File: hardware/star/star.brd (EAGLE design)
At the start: 139.4 x 187.9 mm, 172 parts, among them IC1 MAX481CSA, IC2 LD117AS12TR, IC22 LD117AS12TR, IC3 74HCT08D, IC4 7404D, IC8 MAX481CSA, K1 T90-12VDC-TL-A, K2 T90-12VDC-TL-A, K3 T90-12VDC-TL-A, K5 AQG22110, K6 AQG22110, Q1 35A/25V/8.5mΩ, Q2 35A/25V/8.5mΩ, Q3 35A/25V/8.5mΩ, Q4 35A/25V/8.5mΩ, T1 T_PNP_MMBT5401_CHANGJ_SOT23-B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, T2 T_PNP_MMBT5401_CHANGJ_SOT23-B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, T3 T_PNP_MMBT5401_CHANGJ_SOT23-B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, T4 T_PNP_MMBT5401_CHANGJ_SOT23-B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, U1 TCLT1600

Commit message: Lots of updates
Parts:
- removed C10, C9: C_100UF/6.3V_1206, JLC PCB Basic Parts_loc:C1206
- removed C2, C5: 10uf, rcl:C0603
- removed C24, C26, C4: 1uf, rcl:C0805
- removed F2: 2920L200, 2920L200:SMD050F
- removed JP2: (no value), pinhead:2X02
- removed U$2: ZK-SJVA-4X, Nova:ZK-SJVA-4X
- removed U$3: EPS-25, Nova:EPS-25
- added EPP-120S-24: EPP-120S, Nova:EPS-25
- added NID35-12, NID35-5: NID35, Nova:NID35
- added SKA15B-05: SKA15B, Nova:SKA15B
- IC2: value LD117AS12TR -> 74HCT08D; device v-reg:SOT223 -> 74xx-eu:SO14
- R62: value R_7.5K_0603 -> R_15K_0603
- moved C25 111.1 mm to (134.6, 148.0)
- moved IC2 55.0 mm to (83.2, 65.4)
- moved JP1 51.6 mm to (7.62, 67.3)
- moved C33 35.4 mm to (137.2, 27.9), turned to 90 degrees
- moved I2C 32.4 mm to (132.1, 13.3), turned to 180 degrees
- moved OVERRIDE_EN2 32.1 mm to (126.4, 111.1)
- moved R50 32.0 mm to (121.9, 109.9), turned to 270 degrees
- moved OVERRIDE_EN 31.9 mm to (132.7, 110.5)
- moved IC8 30.5 mm to (133.3, 27.9), turned to 180 degrees
- moved JTAG 28.4 mm to (120.0, 2.54), turned to 180 degrees
- moved 5V_CTRL_LAZERS 20.3 mm to (132.7, 52.7)
- moved C14 20.3 mm to (137.2, 86.4)
- moved D4 20.3 mm to (123.8, 100.3)
- moved IC1 20.3 mm to (133.3, 86.4)
- moved R1 20.3 mm to (137.2, 78.7)
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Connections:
- removed net +14V: C25.1, D14.C, D17.A, FIRE_OUT.3, U$2.OUT+
- removed net N$59: F2.1, POWER_IN.4
- new net +24V: C25.1, D14.C, D17.A, EPP-120S-24.OUT+, FIRE_OUT.3, NID35-12.VIN1, NID35-12.VIN2, NID35-5.VIN1, NID35-5.VIN2, SKA15B-05.+VIN
- new net N$60: IC2.3, Q4.1
- net +12V: now also NID35-12.VOUT1, NID35-12.VOUT2, NID35-12.VOUT3, NID35-12.VOUT4, POWER_IN.4; no longer C2.1, C24.1, C28.+, C35.1, C4.1, C6.1, C89.+, F2.2, IC2.3, IC22.3, U$2.IN+
- net +3V3: now also C28.+, IC2.14
- net +5V: now also C35.1, C6.1, C89.+, IC22.3, NID35-5.VOUT1, NID35-5.VOUT2, NID35-5.VOUT3, NID35-5.VOUT4; no longer C10.1, C5.1, C9.1, IC2.4
- net +5V/2: now also SKA15B-05.+VOUT; no longer C26.1, U$3.OUT+
- net 120_LINE: now also EPP-120S-24.IN-; no longer U$3.IN-
- net 120_NEUTRAL: now also EPP-120S-24.IN+; no longer U$3.IN+
- net 15: now also IC2.2
- net 26_BOOM_IGNITER: now also IC2.1; no longer Q4.1
- net GND: now also EPP-120S-24.OUT-, IC2.7, NID35-12.COM1, NID35-12.COM2, NID35-5.COM1, NID35-5.COM2, SKA15B-05.-VIN; no longer C10.2, C2.2, C24.2, C4.2, C5.2, C9.2, IC2.1, JP2.1, JP2.2, JP2.3, JP2.4, U$2.IN-, U$2.OUT-
- net GND3: now also SKA15B-05.-VOUT; no longer C26.2, U$3.OUT-
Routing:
- net +24V: track 0.00 -> 265.2 mm
- net +12V: track 329.4 -> 149.8 mm
- net +14V: track 106.5 -> 0.00 mm
- net +5V/2: track 128.6 -> 42.2 mm
- net +5V: track 104.2 -> 36.8 mm
- net GND3: track 148.6 -> 86.4 mm
- net +3V3: track 53.8 -> 0.00 mm
- net 120_NEUTRAL: track 180.5 -> 164.3 mm
- net N$59: track 10.2 -> 0.00 mm
- net 120_LINE: track 153.1 -> 146.7 mm
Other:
- board text added: "3v3"
- board text added: "3v3 5v 12v Enable"
- board text added: "ISOLATED 5V"
- board text removed: "12v"
- board text removed: "3v 5v 12v Enable"

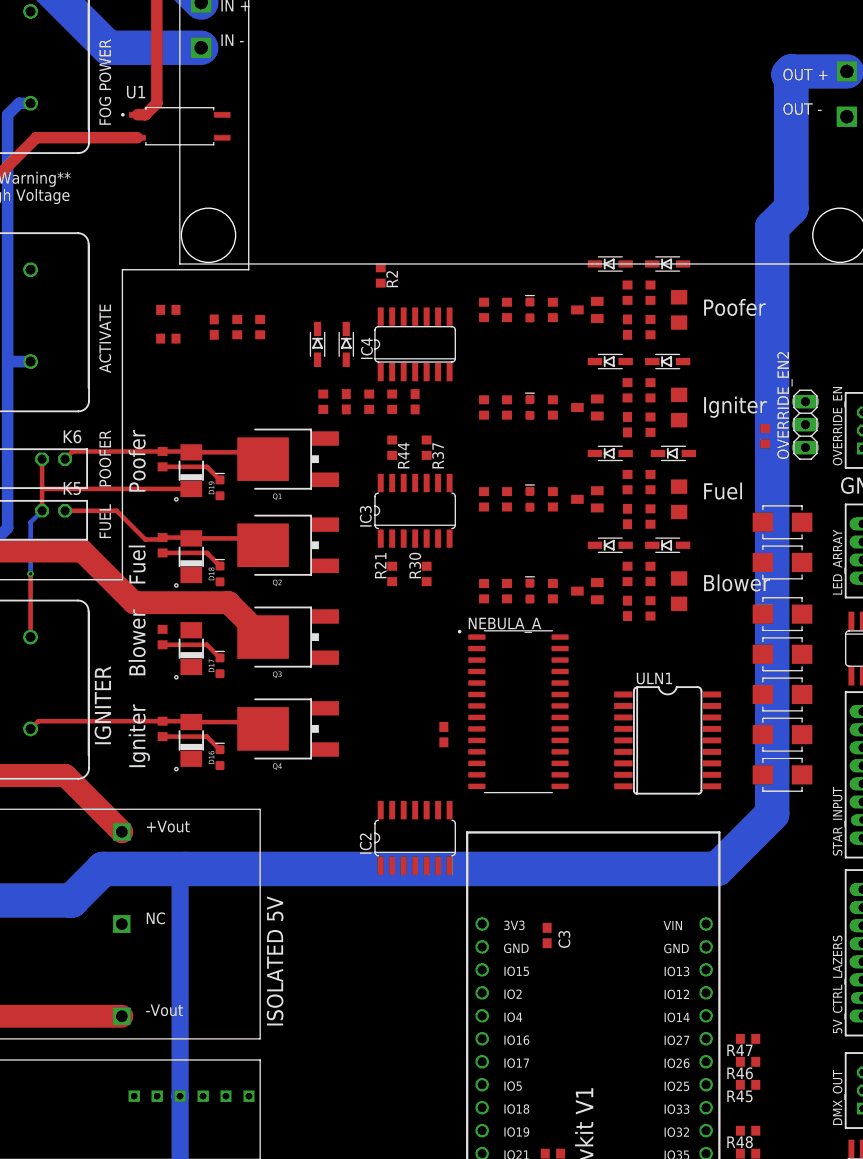
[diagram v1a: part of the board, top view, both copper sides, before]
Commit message: update few traces
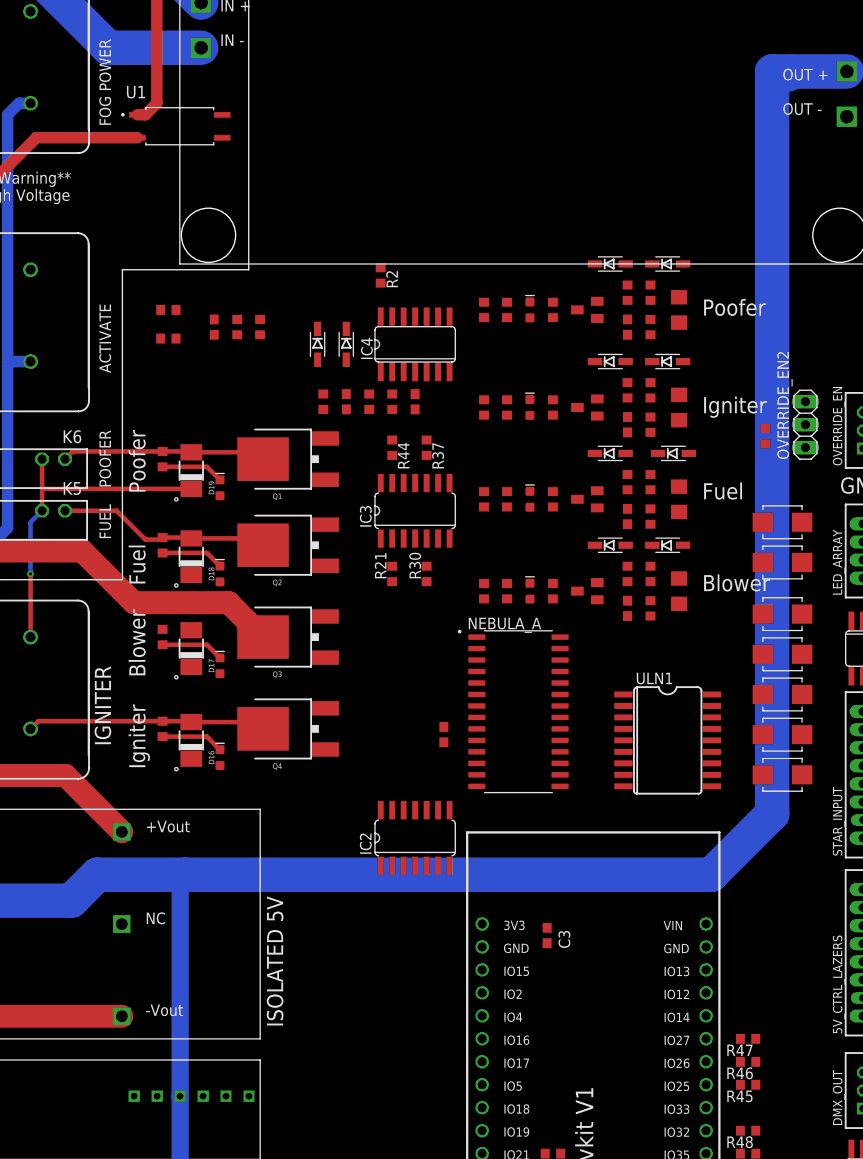
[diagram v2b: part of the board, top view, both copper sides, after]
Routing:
- net +24V: track 265.2 -> 265.8 mm
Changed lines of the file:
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@@
 <contactref element="NID35-12" pad="VIN1"/>
 <wire x1="130.945" y1="150.205" x2="124.805" y2="150.205" width="3.81" layer="16"/>
+<wire x1="124.805" y1="150.205" x2="122.682" y2="150.205" width="3.81" layer="16"/>
 <wire x1="124.46" y1="149.86" x2="124.805" y2="150.205" width="3.81" layer="16"/>
-<wire x1="124.805" y1="150.205" x2="124.805" y2="135.0835625" width="3.81" layer="16"/>
-<wire x1="124.805" y1="135.0835625" x2="122.682" y2="132.9605625" width="3.81" layer="16"/>
-<wire x1="122.682" y1="132.9605625" x2="122.682" y2="68.072" width="3.81" layer="16"/>
+<wire x1="122.682" y1="150.205" x2="122.682" y2="68.072" width="3.81" layer="16"/>
 <wire x1="45.1617125" y1="58.48" x2="30.54" y2="58.48" width="3.81" layer="16"/>
-<wire x1="116.588" y1="61.978" x2="57.785" y2="61.978" width="3.81" layer="16"/>
-<wire x1="57.785" y1="61.978" x2="48.6597125" y2="61.978" width="3.81" layer="16"/>
-<wire x1="48.6597125" y1="61.978" x2="45.1617125" y2="58.48" width="3.81" layer="16"/>
-<wire x1="122.682" y1="68.072" x2="116.588" y2="61.978" width="3.81" layer="16"/>
-<wire x1="57.18" y1="36.845" x2="57.18" y2="61.373" width="1.905" layer="16"/>
-<wire x1="57.18" y1="61.373" x2="57.785" y2="61.978" width="1.905" layer="16"/>
+<wire x1="115.953" y1="61.343" x2="57.785" y2="61.343" width="3.81" layer="16"/>
+<wire x1="57.785" y1="61.343" x2="48.0247125" y2="61.343" width="3.81" layer="16"/>
+<wire x1="48.0247125" y1="61.343" x2="45.1617125" y2="58.48" width="3.81" layer="16"/>
+<wire x1="122.682" y1="68.072" x2="115.953" y2="61.343" width="3.81" layer="16"/>
+<wire x1="57.18" y1="36.845" x2="57.18" y2="60.738" width="1.905" layer="16"/>
+<wire x1="57.18" y1="60.738" x2="57.785" y2="61.343" width="1.905" layer="16"/>
 <wire x1="57.18" y1="36.845" x2="57.18" y2="23.51" width="1.905" layer="16"/>
 <contactref element="D14" pad="C"/>
@@
 <wire x1="54.64" y1="36.845" x2="57.18" y2="36.845" width="0" layer="19" extent="1-1"/>
 <wire x1="54.64" y1="23.51" x2="57.18" y2="23.51" width="0" layer="19" extent="1-1"/>
-<wire x1="134.62" y1="148.905" x2="130.945" y2="150.205" width="0" layer="19" extent="1-1"/>
+<wire x1="134.62" y1="148.905" x2="124.805" y2="150.205" width="0" layer="19" extent="1-1"/>
 </signal>
 <signal name="N$60">

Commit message: Manual routing complete
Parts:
- added X1: MKDSN1,5/2-5,08, con-phoenix-508-jm:MKDSN1,5/2-5,08
- moved POWER_IN 20.3 mm to (7.62, 45.1)
- moved C1 5.08 mm to (125.1, 20.3)
- moved C3 5.08 mm to (102.9, 54.6)
- moved R26 5.08 mm to (103.5, 22.9)
- moved R27 5.08 mm to (103.5, 30.5)
- moved R45 5.08 mm to (125.1, 38.1)
- moved R46 5.08 mm to (125.1, 40.6)
- moved R47 5.08 mm to (125.1, 43.2)
- moved R48 5.08 mm to (125.1, 33.0)
- moved R49 5.08 mm to (125.1, 30.5)
- moved U$1 5.08 mm to (109.2, 33.0)
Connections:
- net +24V: now also X1.2
- net 26_BOOM_IGNITER: now also Q4.1; no longer IC2.1
- net 32_BOOM_BLOWER: now also IC2.1; no longer Q3.1
- net GND: now also X1.1
- net N$60: now also Q3.1; no longer Q4.1
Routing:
- net +5V: track 36.8 -> 218.3 mm
- net GND3: track 86.4 -> 0.00 mm
- net +24V: track 265.8 -> 320.1 mm
- net +3V3: track 0.00 -> 50.2 mm
- net +12V: track 149.8 -> 171.9 mm
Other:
- board text added: "GND 24v"
- board text removed: "120vac IN"
- board text removed: "GND 5v/2"

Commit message: starbase v02
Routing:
- net +3V3: track 50.2 -> 504.9 mm, vias 0 -> 11
- net GND: track 0.30 -> 426.1 mm, vias 0 -> 12
- net +5V: track 218.3 -> 501.0 mm, vias 1 -> 3
- net EXP_ULN1: track 0.00 -> 198.2 mm, vias 0 -> 3
- net LOCAL_EN: track 0.00 -> 175.9 mm, vias 0 -> 4
- net EXP_ULN0: track 0.00 -> 164.1 mm, vias 0 -> 2
- net +12V: track 171.9 -> 327.7 mm, vias 0 -> 5
- net EN_STATUS: track 0.00 -> 155.8 mm, vias 0 -> 2
- net A0: track 0.00 -> 148.4 mm, vias 0 -> 2
- net 19: track 0.00 -> 128.0 mm
- net 18: track 0.00 -> 117.9 mm
- net 21/SDA: track 0.00 -> 103.2 mm
- net 22/SCL: track 0.00 -> 93.9 mm, vias 0 -> 1
- net 25_POOFER: track 0.00 -> 91.4 mm, vias 0 -> 2
- net N$4: track 0.00 -> 89.9 mm, vias 0 -> 2
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
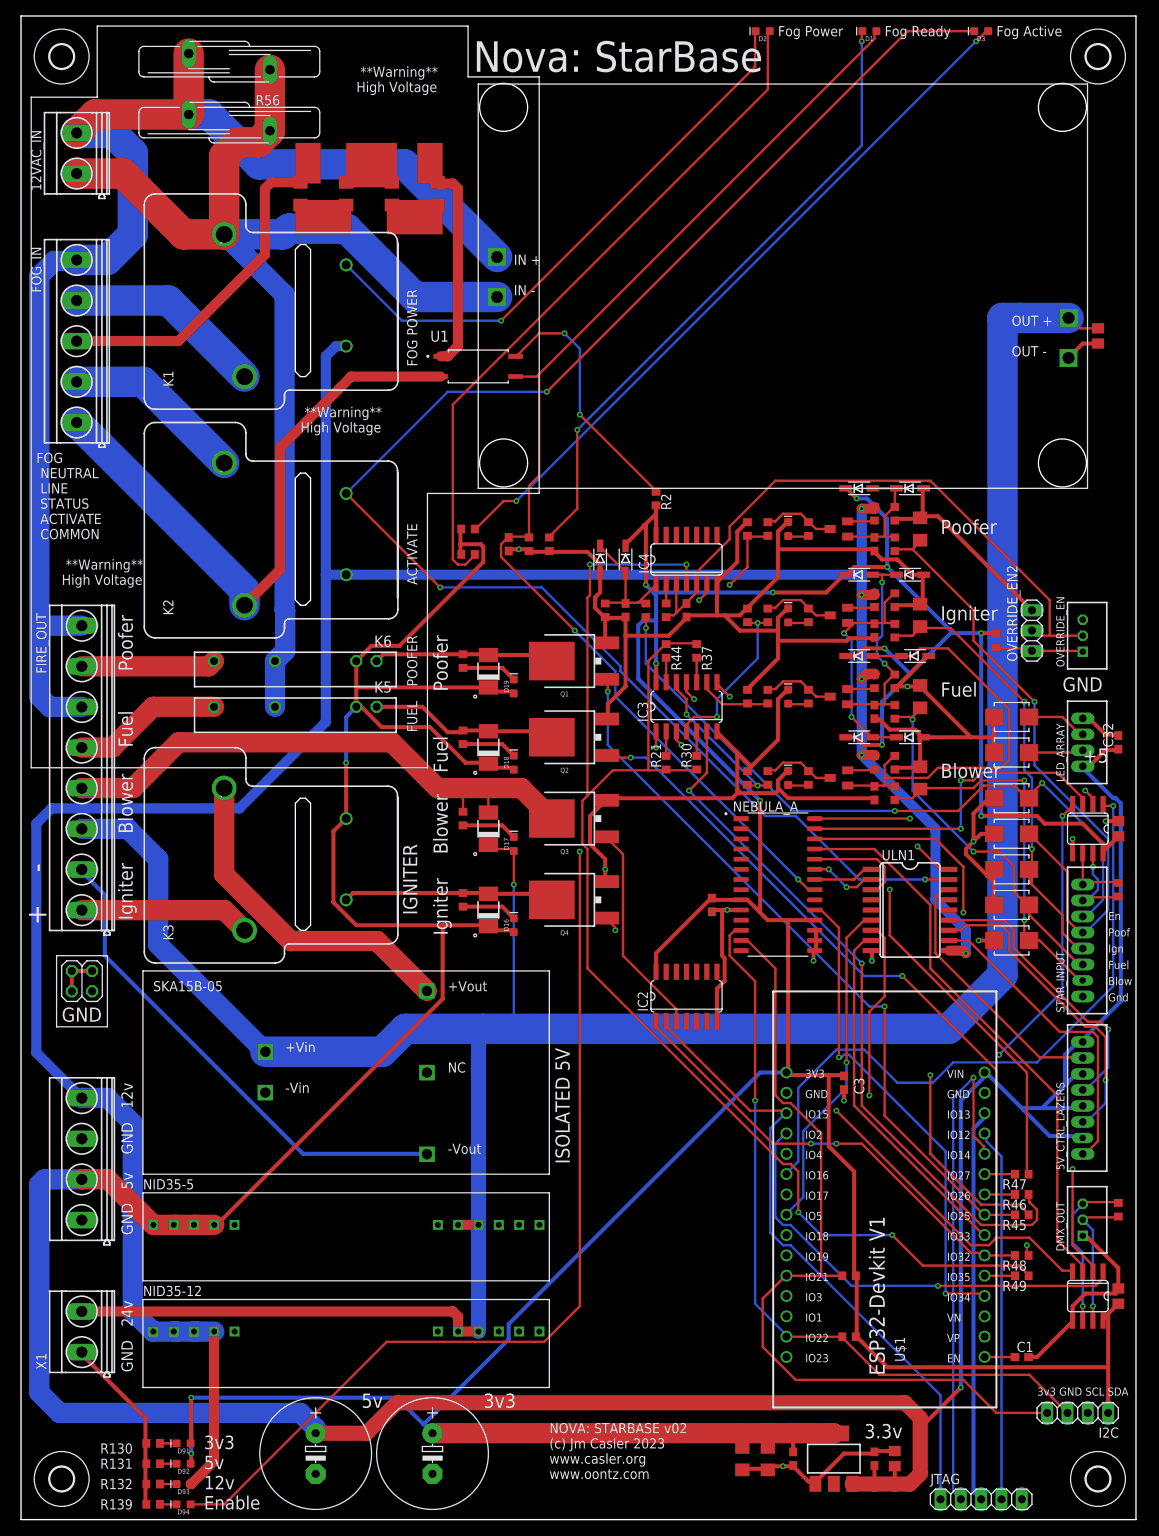
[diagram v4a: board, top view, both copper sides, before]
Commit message: swap to schmitt trigger
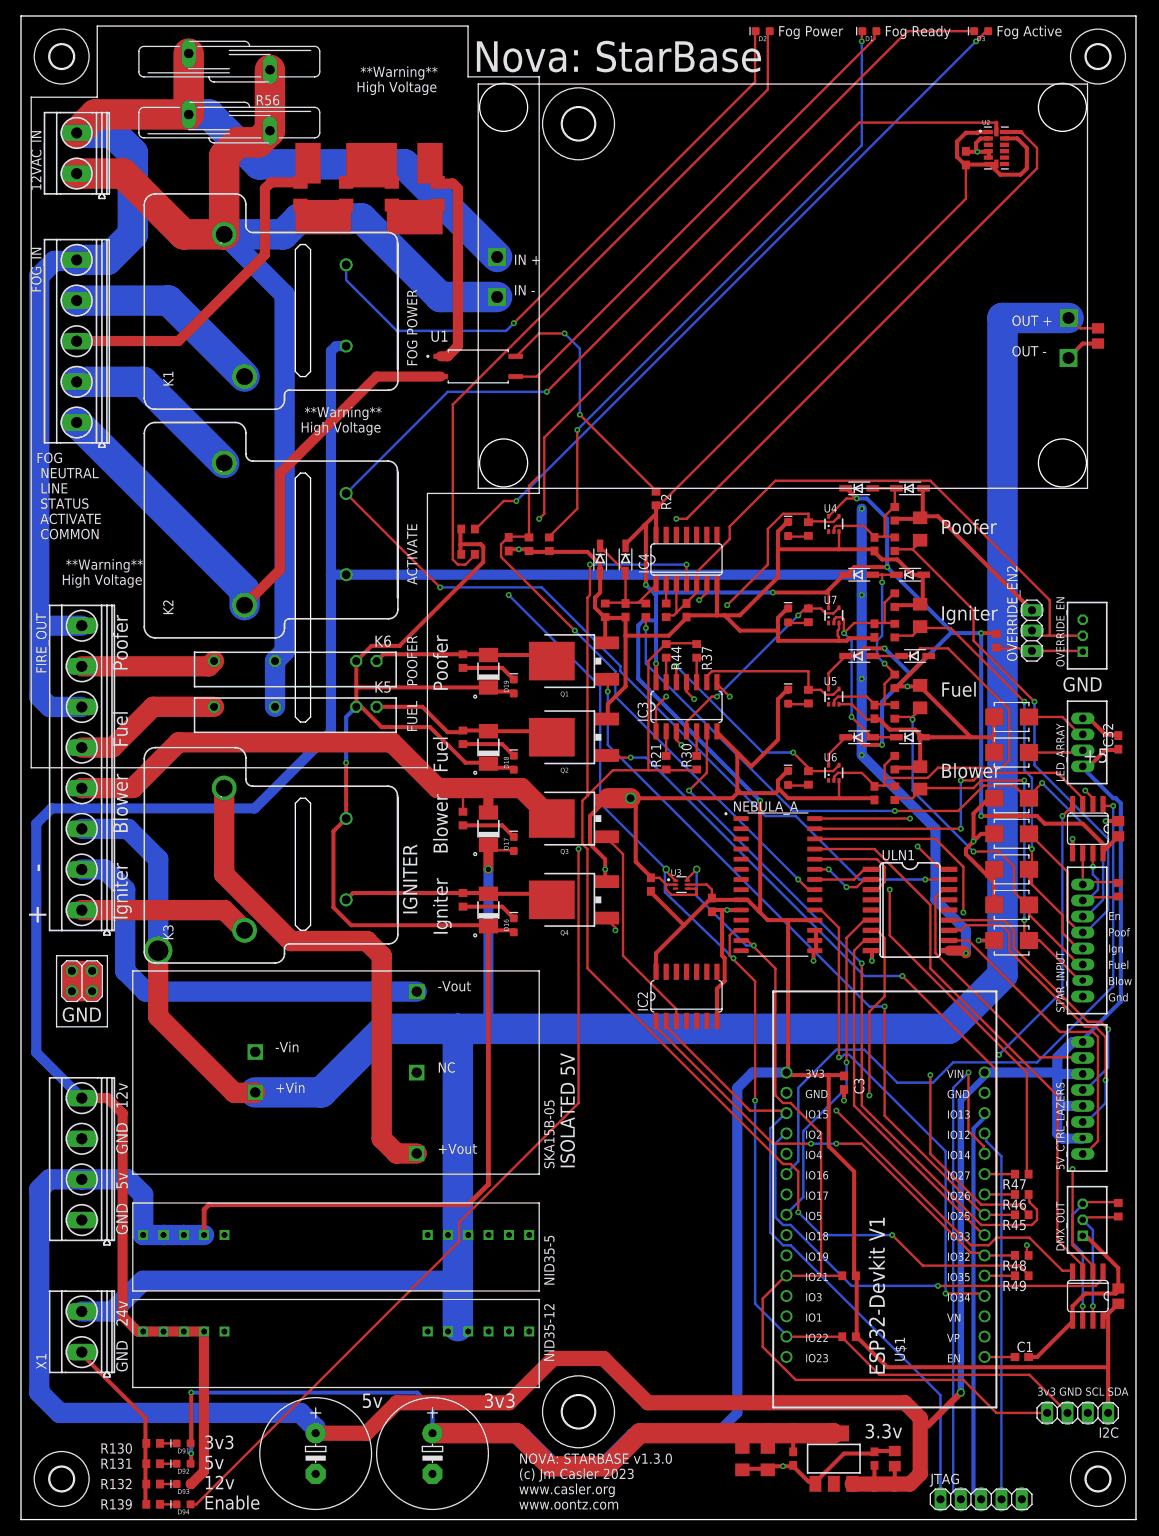
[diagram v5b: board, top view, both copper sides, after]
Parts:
- removed R15, R24, R33, R40: R_10R_0603, JLC PCB Basic Parts_loc:R0603
- removed R17, R28, R35, R42: R_2.7K_0603, JLC PCB Basic Parts_loc:R0603
- removed R18, R29, R36, R43: R_1K_0603, JLC PCB Basic Parts_loc:R0603
- removed T1, T2, T3, T4: T_PNP_MMBT5401_CHANGJ_SOT23-BEC, JLC PCB Basic Parts_loc:SOT23
- added C2, C4: C_1UF/50V_0603, JLC PCB Basic Parts_loc:C0603
- added H5, H6: MOUNT-HOLE4.1, holes:4,1
- added U2: ADXL343BCCZ-RL7, ADXL343BCCZ-RL7:PQFN80P300X500X100-14N
- added U3: TMP102AIDRLR, TMP102AIDRLR:SOT50P160X60-6N
- added U4, U5, U6, U7: SN74LVC1G17DCK, SN74LVC1G17:SC70-5
- R16, R25, R34, R41: value R_12K_0603 -> R_1K_0603
- moved NID35-5 1.80 mm to (14.0, 28.6)
- moved NID35-12 1.27 mm to (14.0, 16.5)
- moved SKA15B-05 1.27 mm to (14.0, 43.2)
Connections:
- removed net N$19: IC3.1, R17.1, R18.2
- removed net N$20: R15.1, T1.2
- removed net N$28: IC3.4, R28.1, R29.2
- removed net N$29: R24.1, T2.2
- removed net N$34: IC3.9, R35.1, R36.2
- removed net N$35: R33.1, T3.2
- removed net N$40: IC3.12, R42.1, R43.2
- removed net N$41: R40.1, T4.2
- net +12V: no longer R15.2, R24.2, R33.2, R40.2
- net +3V3: now also C2.1, C4.1, U2.1, U2.12, U2.6, U2.7, U3.5, U4.5, U5.5, U6.5, U7.5
- net 21/SDA: now also U2.13, U3.6
- net 22/SCL: now also U2.14, U3.1
- net GND: now also C2.2, C4.2, U2.2, U2.4, U2.5, U3.2, U3.4, U4.3, U5.3, U6.3, U7.3; no longer R18.1, R29.1, R36.1, R43.1
- net N$16: now also IC3.1, U4.4; no longer R17.2, T1.3
- net N$17: now also U4.2; no longer T1.1
- net N$25: now also U7.2; no longer T2.1
- net N$26: now also IC3.4, U7.4; no longer R28.2, T2.3
- net N$31: now also U5.2; no longer T3.1
- net N$32: now also IC3.9, U5.4; no longer R35.2, T3.3
- net N$37: now also U6.2; no longer T4.1
- net N$38: now also IC3.12, U6.4; no longer R42.2, T4.3
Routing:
- net 22/SCL: track 93.9 -> 248.7 mm, vias 1 -> 5
- net 21/SDA: track 103.2 -> 253.2 mm, vias 0 -> 3
- net +3V3: track 504.9 -> 645.4 mm
- net N$19: track 35.8 -> 0.00 mm, vias 2 -> 0
- net N$16: track 9.18 -> 42.3 mm, vias 0 -> 2
- net GND: track 426.1 -> 452.3 mm, vias 12 -> 14
- net +5V: track 501.0 -> 525.7 mm
- net N$28: track 21.7 -> 0.00 mm, vias 2 -> 0
- net +5V/2: track 42.2 -> 62.7 mm
- net N$40: track 19.9 -> 0.00 mm, vias 2 -> 0
- net N$38: track 9.18 -> 28.3 mm, vias 0 -> 2
- net N$26: track 9.18 -> 27.2 mm, vias 0 -> 2
- net EN_STATUS: track 155.8 -> 142.2 mm
- net N$32: track 9.18 -> 20.4 mm
- net +24V: track 349.8 -> 359.9 mm, vias 1 -> 2
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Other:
- outline, holes or cut-outs redrawn
- board text added: "NOVA: STARBASE v1.3.0 (c) Jm Casler 2023 www.casler.org www.oontz.com"
- board text removed: "NOVA: STARBASE v02 (c) Jm Casler 2023 www.casler.org www.oontz.com"
